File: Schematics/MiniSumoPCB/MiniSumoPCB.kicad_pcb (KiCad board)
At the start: 2 copper layers, 65 x 55 mm, 69 parts, among them J1 Alimentacion, J10 TOF_F, J11 TOF_FR, J12 TOF_FL, J13 TOF_L, J14 TOF_R, J15 TOF_B, J16 EXTRA_I2C1, J17 EXTRA_I2C2, J18 Servo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

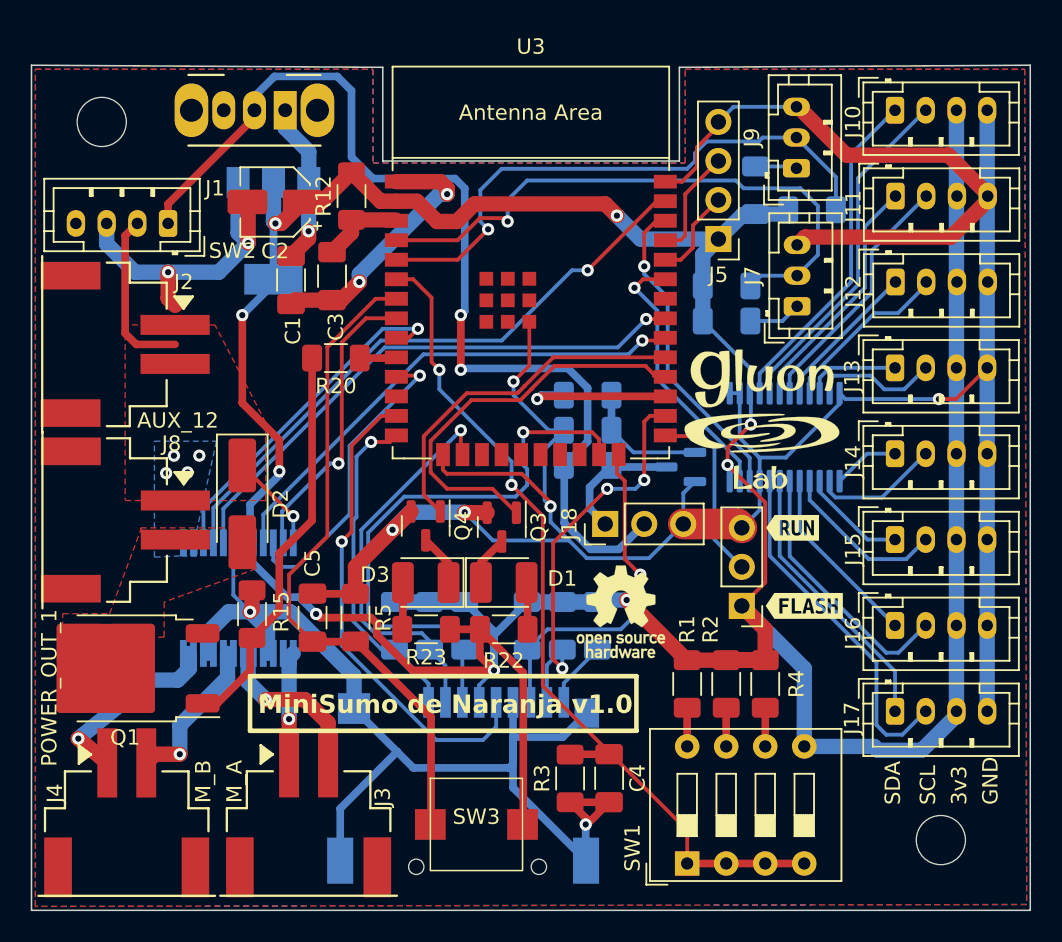
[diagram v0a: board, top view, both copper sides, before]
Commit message: [PCB] Added decoupling Capacitors
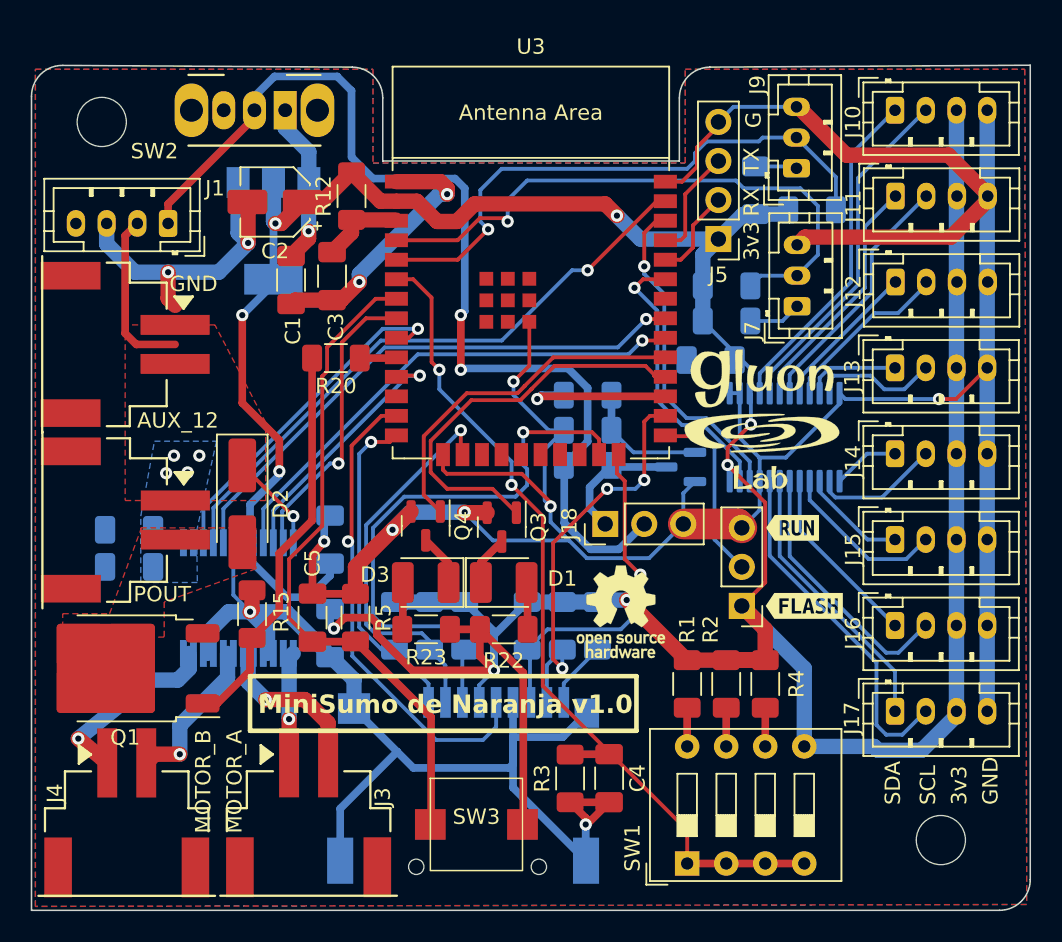
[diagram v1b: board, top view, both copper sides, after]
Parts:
- added C11: 100nF, Capacitor_SMD:C_1206_3216Metric_Pad1.33x1.80mm_HandSolder, B.Cu at (157.2, 63.5)
- added C6: 100nF, Capacitor_SMD:C_1206_3216Metric_Pad1.33x1.80mm_HandSolder, B.Cu at (132.5, 75.2)
- added C7: 10u, Capacitor_SMD:C_1206_3216Metric_Pad1.33x1.80mm_HandSolder, B.Cu at (132.5, 81.3)
- added C8: 10u, Capacitor_SMD:C_1206_3216Metric_Pad1.33x1.80mm_HandSolder, B.Cu at (119.4, 74.6)
- added C9: 100nF, Capacitor_SMD:C_1206_3216Metric_Pad1.33x1.80mm_HandSolder, B.Cu at (119.4, 77.0)
- J3: value M_A -> MOTOR_A
- J4: value M_B -> MOTOR_B
- J8: value POWER_OUT_1 -> POUT
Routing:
- net GND: track 288.6 -> 294.0 mm, vias 11 -> 12
- net +3V3: track 235.9 -> 239.9 mm
- net MOTOR_A_IN2: track 20.2 -> 16.8 mm
- net TCA_SDA: track 17.7 -> 18.5 mm
- net TCA_SCL: track 20.7 -> 21.5 mm
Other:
- outline, holes or cut-outs redrawn
- board text added: "G"
- board text added: "RX"
- board text added: "TX"
- board text added: "araba_st spuertes andygm_ vitorio08 carlosbetdev jfelipe_mg gorn6_ fisitronics david_wiki humiltat pipermind famedst txusev raupulus zurano_ un_bizco"
- board text removed: "araba_st spuertes andygm_ vitorio08 carlosbetdev jfelipe_mg gorn6_ fisitronics david_wiki humiltat pipermind famedst txusev raupulus zurano_"

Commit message: [PCB] Update minor version
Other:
- board text added: "MiniSumo de Naranja v1.1"
- board text removed: "MiniSumo de Naranja v1.0"
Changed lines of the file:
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@@
     (effects (font (size 1 1) (thickness 0.15)) (justify left bottom))
   )
-  (gr_text "MiniSumo de Naranja v1.0" (at 127.762 86.652) (layer "F.SilkS")
+  (gr_text "MiniSumo de Naranja v1.1" (at 127.762 86.652) (layer "F.SilkS")
     (effects (font (size 1.2 1.2) (thickness 0.2) bold) (justify left bottom))
   )
